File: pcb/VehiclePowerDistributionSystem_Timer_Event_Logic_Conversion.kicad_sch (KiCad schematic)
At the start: 4 parts

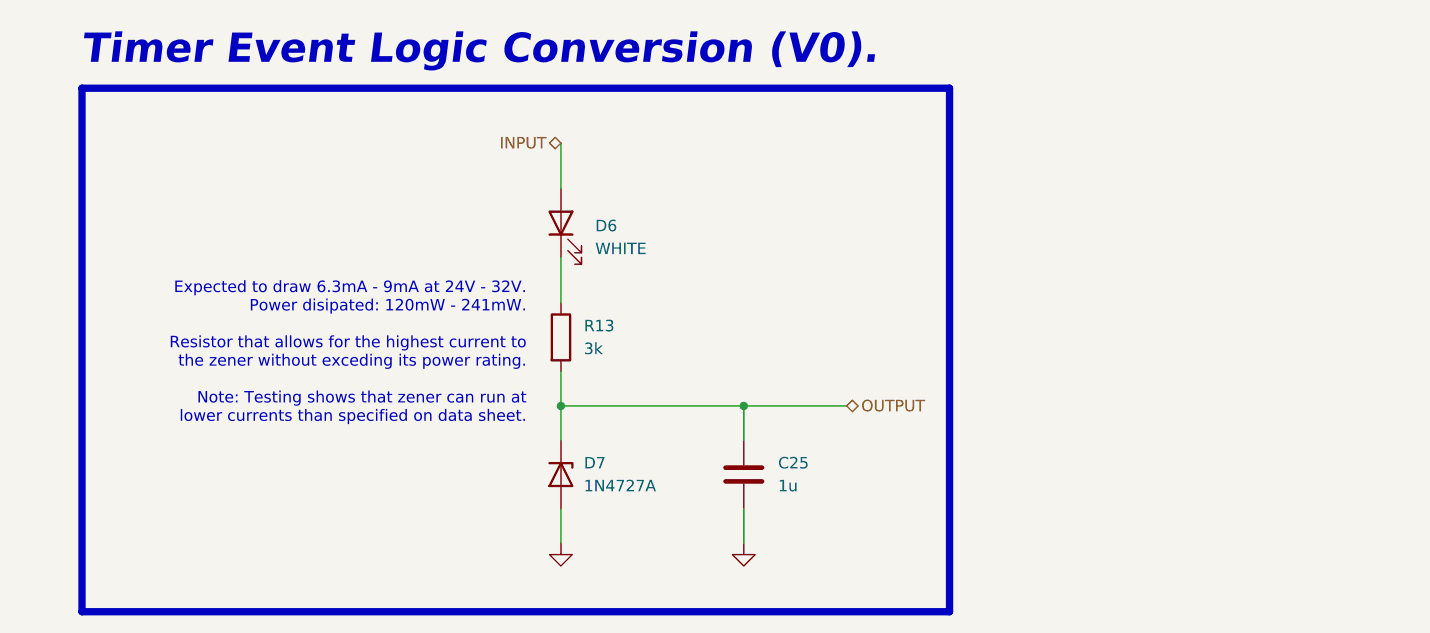
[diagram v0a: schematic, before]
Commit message: Geographically reannotated `VehiclePowerDistributionSystem`.
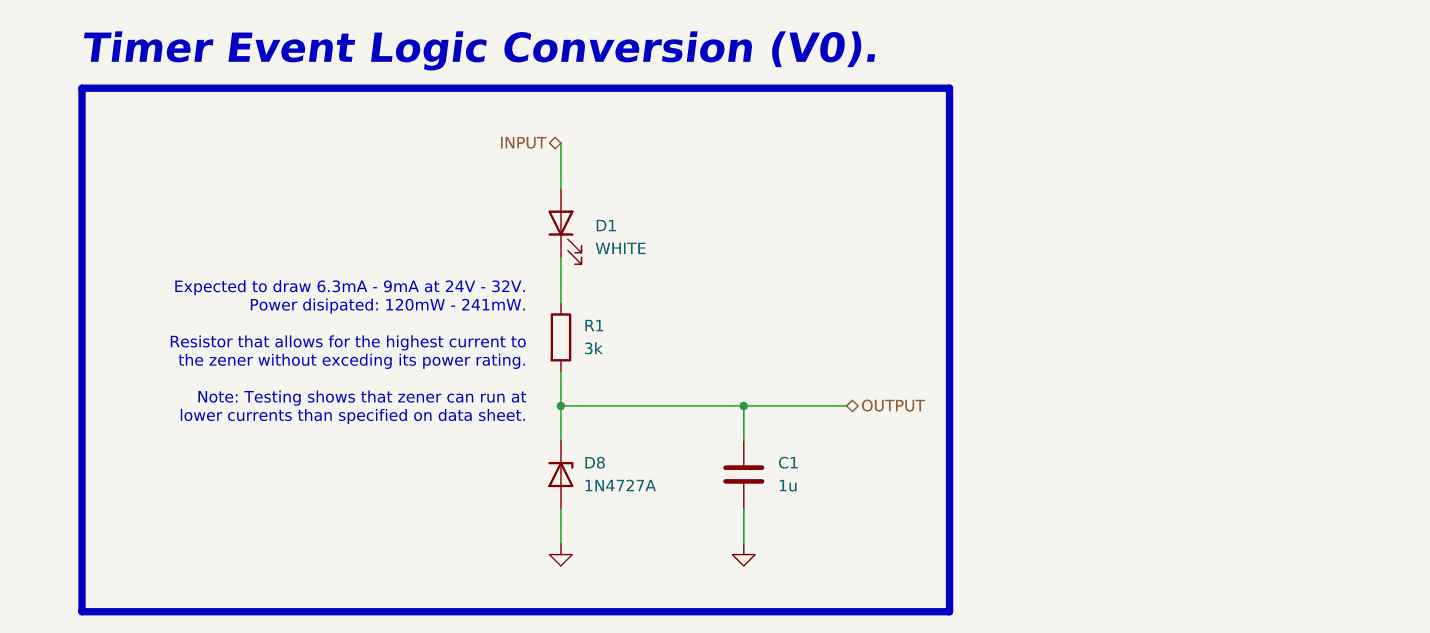
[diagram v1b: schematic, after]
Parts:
- renumbered C25 to C1, D6 to D1, D7 to D8, R13 to R1
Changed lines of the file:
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@@
 		(dnp no)
 		(fields_autoplaced yes)
-		(property "Reference" "C25"
+		(property "Reference" "C1"
 			(at 138.43 91.4399 0)
 			(effects
@@
 			(project "VehiclePowerDistributionSystem"
 				(path "/92a7a41c-8494-4e4b-ac2d-deb1f1cd8085/54620fe3-2093-4758-a776-838cd07d45c6"
-					(reference "C25")
+					(reference "C1")
 					(unit 1)
 				)
@@
 		(dnp no)
 		(fields_autoplaced yes)
-		(property "Reference" "D6"
+		(property "Reference" "D1"
 			(at 118.11 65.0874 90)
 			(effects
@@
 			(project "VehiclePowerDistributionSystem"
 				(path "/92a7a41c-8494-4e4b-ac2d-deb1f1cd8085/54620fe3-2093-4758-a776-838cd07d45c6"
-					(reference "D6")
+					(reference "D1")
 					(unit 1)
 				)
@@
 		(dnp no)
 		(fields_autoplaced yes)
-		(property "Reference" "R13"
+		(property "Reference" "R1"
 			(at 116.84 76.1999 0)
 			(effects
@@
 			(project "VehiclePowerDistributionSystem"
 				(path "/92a7a41c-8494-4e4b-ac2d-deb1f1cd8085/54620fe3-2093-4758-a776-838cd07d45c6"
-					(reference "R13")
+					(reference "R1")
 					(unit 1)
 				)
@@
 		(dnp no)
 		(fields_autoplaced yes)
-		(property "Reference" "D7"
+		(property "Reference" "D8"
 			(at 116.84 91.4399 90)
 			(effects
@@
 			(project "VehiclePowerDistributionSystem"
 				(path "/92a7a41c-8494-4e4b-ac2d-deb1f1cd8085/54620fe3-2093-4758-a776-838cd07d45c6"
-					(reference "D7")
-					(unit 1)
-				)
+					(reference "D8")
+					(unit 1)
+				)

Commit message: Deprecated `motor_uart_rx` for `VehicleFlightComputer` and `VehiclePowerDistributionSystem`.
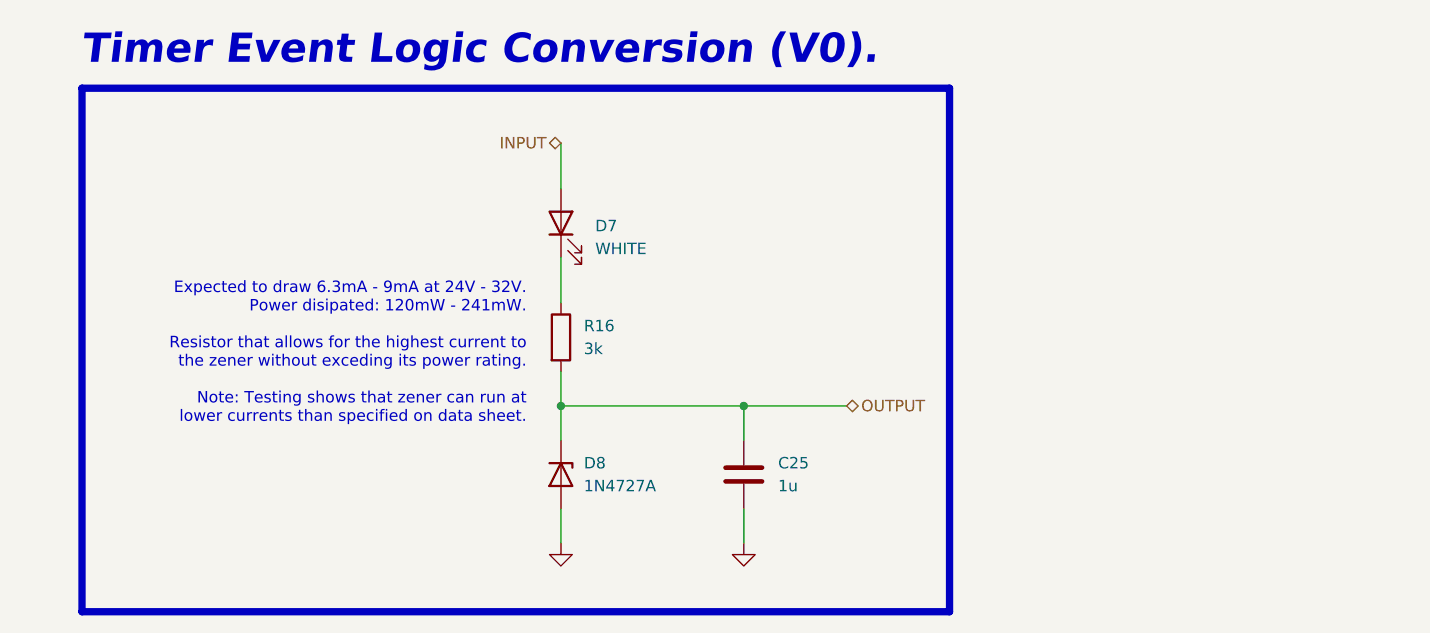
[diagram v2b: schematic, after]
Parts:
- renumbered C1 to C25, D1 to D7, R1 to R16
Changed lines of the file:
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@@
 		(dnp no)
 		(fields_autoplaced yes)
-		(property "Reference" "C1"
+		(property "Reference" "C25"
 			(at 138.43 91.4399 0)
 			(effects
@@
 			(project "VehiclePowerDistributionSystem"
 				(path "/92a7a41c-8494-4e4b-ac2d-deb1f1cd8085/54620fe3-2093-4758-a776-838cd07d45c6"
-					(reference "C1")
+					(reference "C25")
 					(unit 1)
 				)
@@
 		(dnp no)
 		(fields_autoplaced yes)
-		(property "Reference" "#PWR014"
+		(property "Reference" "#PWR080"
 			(at 114.3 106.68 0)
 			(effects
@@
 			(project "VehiclePowerDistributionSystem"
 				(path "/92a7a41c-8494-4e4b-ac2d-deb1f1cd8085/54620fe3-2093-4758-a776-838cd07d45c6"
-					(reference "#PWR014")
+					(reference "#PWR080")
 					(unit 1)
 				)
@@
 		(dnp no)
 		(fields_autoplaced yes)
-		(property "Reference" "D1"
+		(property "Reference" "D7"
 			(at 118.11 65.0874 90)
 			(effects
@@
 			(project "VehiclePowerDistributionSystem"
 				(path "/92a7a41c-8494-4e4b-ac2d-deb1f1cd8085/54620fe3-2093-4758-a776-838cd07d45c6"
-					(reference "D1")
+					(reference "D7")
 					(unit 1)
 				)
@@
 		(dnp no)
 		(fields_autoplaced yes)
-		(property "Reference" "R1"
+		(property "Reference" "R16"
 			(at 116.84 76.1999 0)
 			(effects
@@
 			(project "VehiclePowerDistributionSystem"
 				(path "/92a7a41c-8494-4e4b-ac2d-deb1f1cd8085/54620fe3-2093-4758-a776-838cd07d45c6"
-					(reference "R1")
+					(reference "R16")
 					(unit 1)
 				)
@@
 		(dnp no)
 		(fields_autoplaced yes)
-		(property "Reference" "#PWR015"
+		(property "Reference" "#PWR081"
 			(at 134.62 106.68 0)
 			(effects
@@
 			(project "VehiclePowerDistributionSystem"
 				(path "/92a7a41c-8494-4e4b-ac2d-deb1f1cd8085/54620fe3-2093-4758-a776-838cd07d45c6"
-					(reference "#PWR015")
-					(unit 1)
-				)
+					(reference "#PWR081")
+					(unit 1)
+				)

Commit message: Updated `Timer_Event_Logic_Conversion` design block.
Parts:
- removed C25: 1u, Capacitor_SMD:C_1206_3216Metric_Pad1.33x1.80mm_HandSolder, symbol Device:C
- added R17: 100k, Resistor_SMD:R_1206_3216Metric_Pad1.30x1.75mm_HandSolder, symbol Device:R
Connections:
- net GND: now also R17.2
- net INPUT: now also R17.1
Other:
- note added: "Acts as a drain for stray current."
- note added: "Timer Event Logic Conversion (V1 : Pull-down)."
- note removed: "Expected to draw 6.3mA - 9mA at 24V - 32V. Power disipated: 120mW - 241mW. Resistor that allows for the highest current to the zener without exceding its power rating. Note: Testing shows that zener can run at lower currents than specified on data sheet."
- note removed: "Timer Event Logic Conversion (V0)."
- moved on the sheet: D7, D8, R16

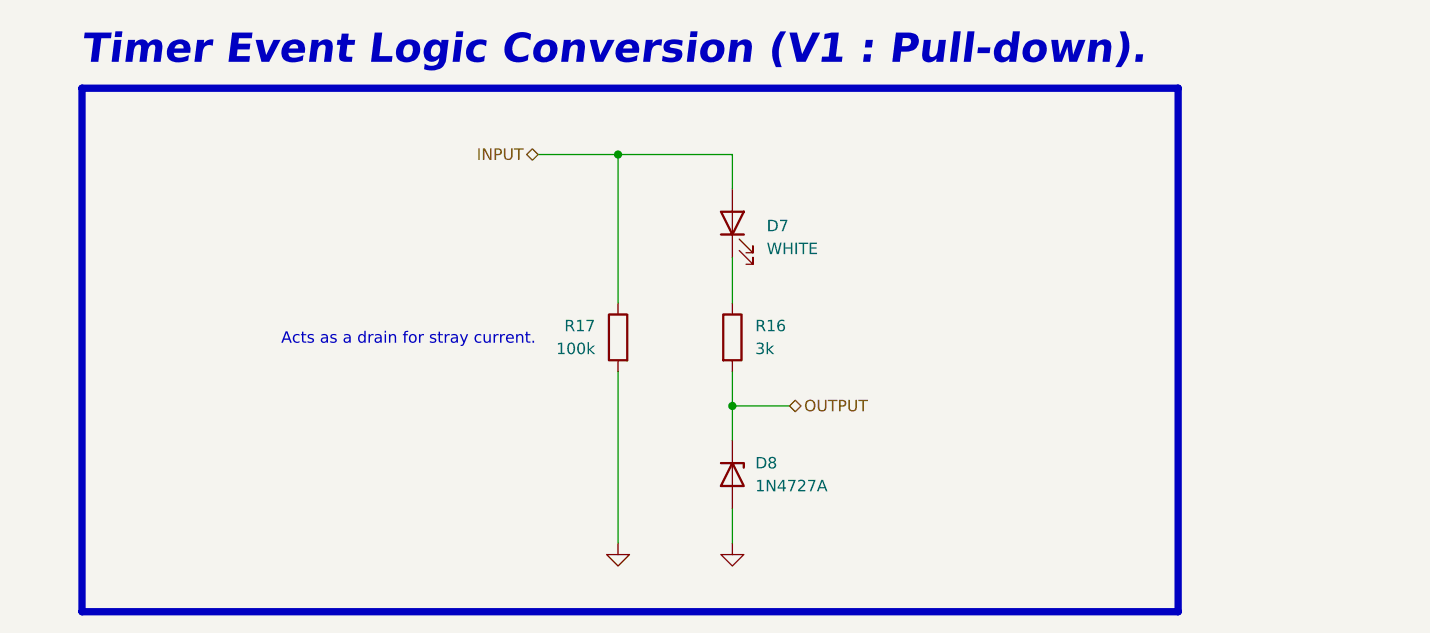
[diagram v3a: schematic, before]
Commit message: Revised `VehiclePowerDistributionSystem`.
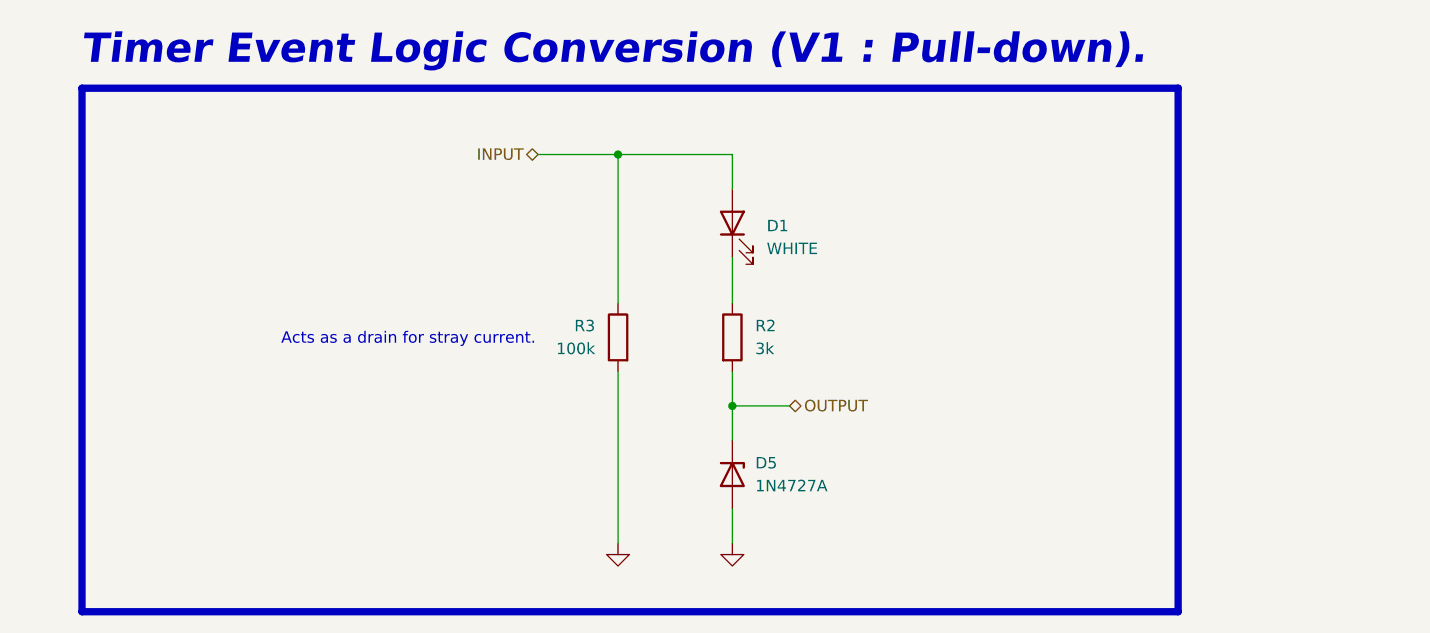
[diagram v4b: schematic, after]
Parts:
- renumbered D7 to D1, D8 to D5, R16 to R2, R17 to R3
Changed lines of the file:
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@@
 		(dnp no)
 		(fields_autoplaced yes)
-		(property "Reference" "D7"
+		(property "Reference" "D1"
 			(at 137.16 65.0874 90)
 			(effects
@@
 			(project "VehiclePowerDistributionSystem"
 				(path "/92a7a41c-8494-4e4b-ac2d-deb1f1cd8085/54620fe3-2093-4758-a776-838cd07d45c6"
-					(reference "D7")
+					(reference "D1")
 					(unit 1)
 				)
@@
 		(on_board yes)
 		(dnp no)
-		(property "Reference" "R17"
+		(property "Reference" "R3"
 			(at 118.11 76.1999 0)
 			(effects
@@
 			(project "VehiclePowerDistributionSystem"
 				(path "/92a7a41c-8494-4e4b-ac2d-deb1f1cd8085/54620fe3-2093-4758-a776-838cd07d45c6"
-					(reference "R17")
+					(reference "R3")
 					(unit 1)
 				)
@@
 		(dnp no)
 		(fields_autoplaced yes)
-		(property "Reference" "R16"
+		(property "Reference" "R2"
 			(at 135.89 76.1999 0)
 			(effects
@@
 			(project "VehiclePowerDistributionSystem"
 				(path "/92a7a41c-8494-4e4b-ac2d-deb1f1cd8085/54620fe3-2093-4758-a776-838cd07d45c6"
-					(reference "R16")
+					(reference "R2")
 					(unit 1)
 				)
@@
 		(dnp no)
 		(fields_autoplaced yes)
-		(property "Reference" "D8"
+		(property "Reference" "D5"
 			(at 135.89 91.4399 90)
 			(effects
@@
 			(project "VehiclePowerDistributionSystem"
 				(path "/92a7a41c-8494-4e4b-ac2d-deb1f1cd8085/54620fe3-2093-4758-a776-838cd07d45c6"
-					(reference "D8")
-					(unit 1)
-				)
+					(reference "D5")
+					(unit 1)
+				)
